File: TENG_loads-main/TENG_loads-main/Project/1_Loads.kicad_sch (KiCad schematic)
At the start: 7 parts, among them IC11 74HC238D,653, IC2 TBD62083AFG, IC3 TBD62083AFG

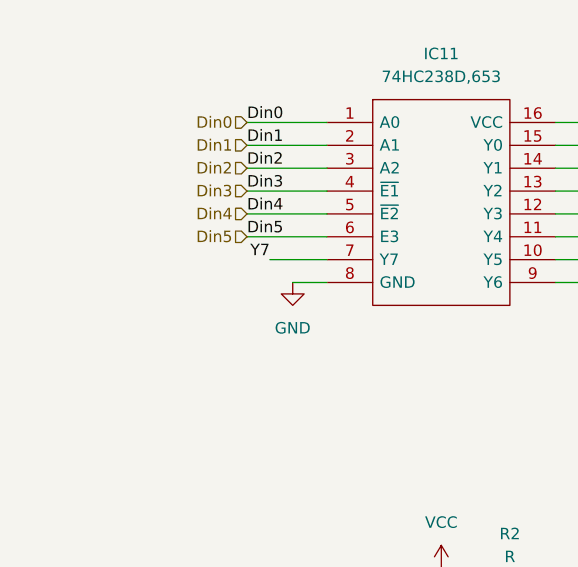
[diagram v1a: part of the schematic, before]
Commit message: Pull Down Resistor and reconnect
Introduced the pull down resistors and reconnect all the unconnected tracks. The position of some items has changed to fit the new components.
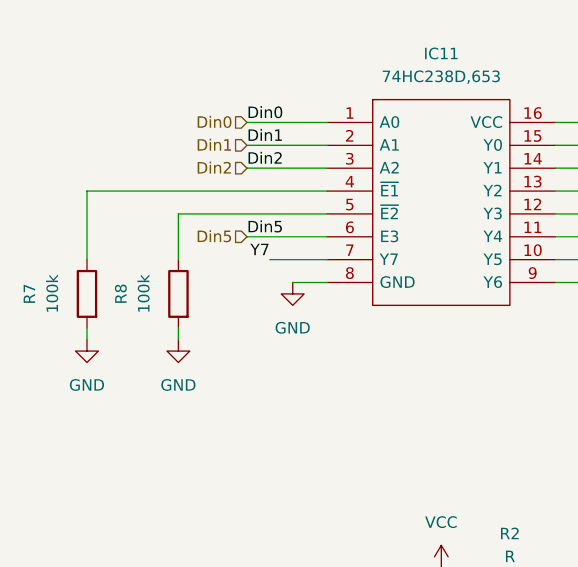
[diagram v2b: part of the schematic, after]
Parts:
- added R7, R8: 100k, Resistor_SMD:R_0805_2012Metric, symbol Device:R
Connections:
- net GND: now also R7.2, R8.2
- net Din3: no longer names the net of IC11.4 (~{E1})
- net Din3: now also R7.1
- net Din4: no longer names the net of IC11.5 (~{E2})
- net Din4: now also R8.1
